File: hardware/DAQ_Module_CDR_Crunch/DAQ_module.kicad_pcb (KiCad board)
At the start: 4 copper layers, 38 x 58.5 mm, 56 parts, among them J1 Conn_01x10_Pin, J3 Conn_01x20_Pin, U1 MCP3564RT-E/ST, U2 MAX31855KASA, U3 MAX31855KASA, U5 TPS70933DBVR, U6 TPS70933DBVR, U7 TPS70933DBVR, U8 MAX31855KASA

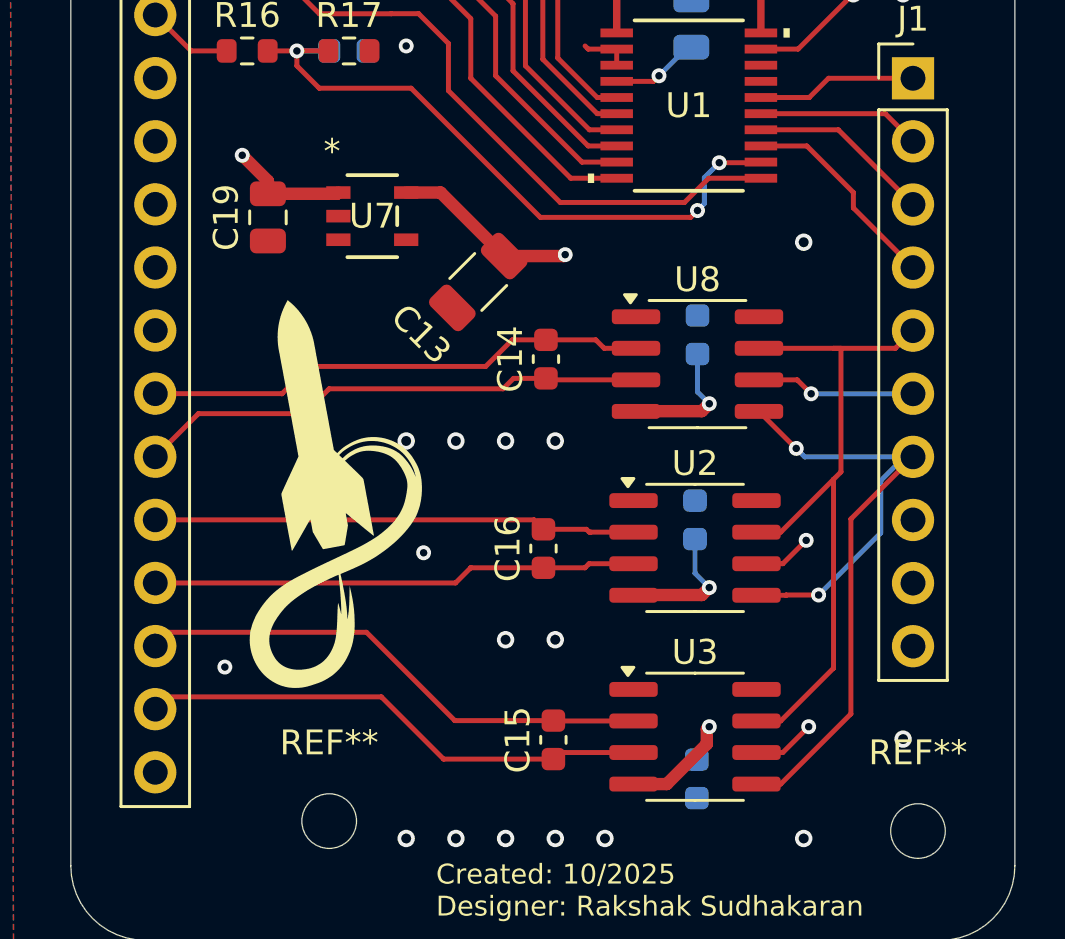
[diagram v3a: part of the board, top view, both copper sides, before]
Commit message: Fixed some traces' layer selection
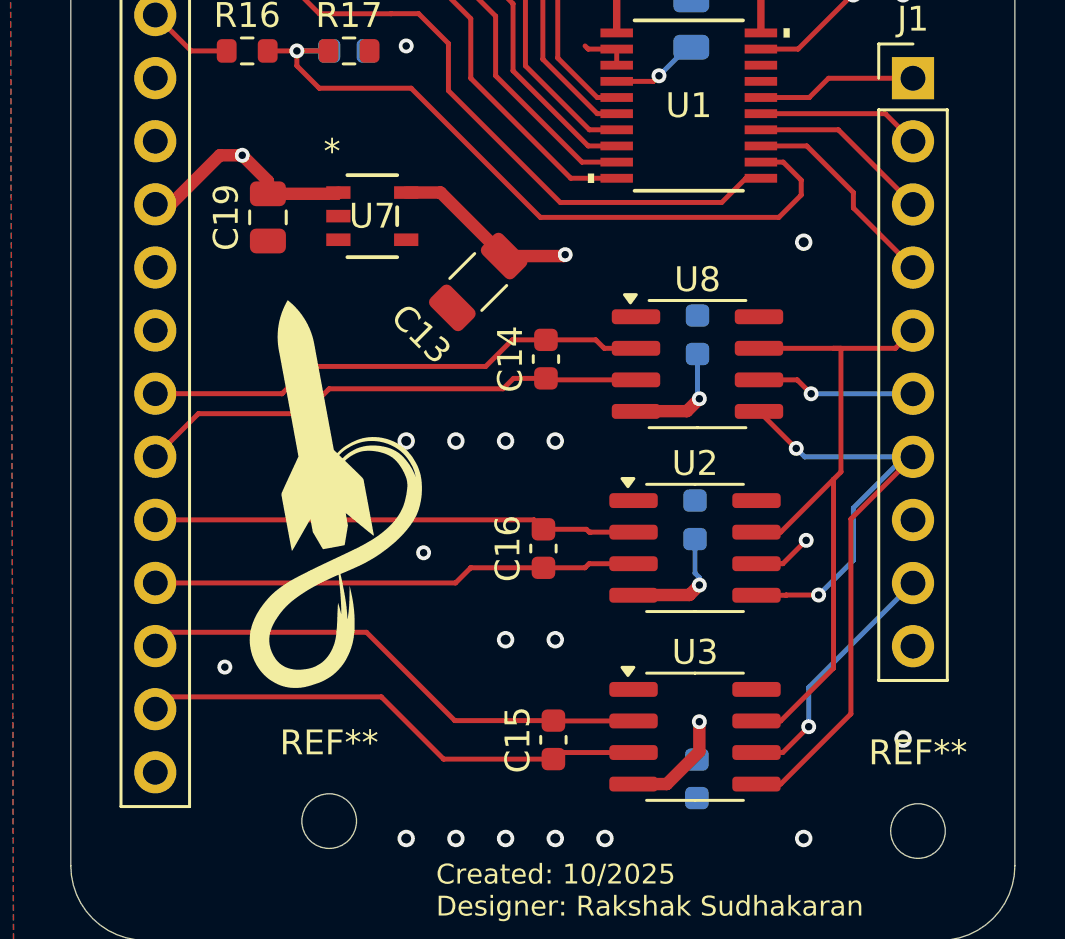
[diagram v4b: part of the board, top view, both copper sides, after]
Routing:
- net /ADC_AI_Filt_7: track 27.1 -> 30.1 mm, vias 3 -> 1
- net Net-(U2-V_{CC}): track 47.9 -> 46.3 mm

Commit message: Updated silkscreen text
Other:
- board text added: "Created: 10/2025 Designer: Rakshak Sudhakaran Board: DAQ Module"
- board text removed: "Created: 10/2025 Designer: Rakshak Sudhakaran"
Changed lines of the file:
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@@
 		(tags "resistor")
 		(property "Reference" "R7"
-			(at 0 -1.43 0)
+			(at 0 1.5 0)
 			(layer "F.SilkS")
 			(effects
@@
 		(tags "resistor")
 		(property "Reference" "R4"
-			(at 0 -1.43 0)
+			(at 0 1.5 0)
 			(layer "F.SilkS")
 			(effects
@@
 		(tags "resistor")
 		(property "Reference" "R2"
-			(at 0 -1.43 0)
+			(at 0 1.5 0)
 			(layer "F.SilkS")
 			(effects
@@
 		(tags "capacitor")
 		(property "Reference" "C2"
-			(at 0 -1.68 0)
+			(at 2.55 1.8 0)
 			(layer "F.SilkS")
 			(effects
@@
 		(tags "resistor")
 		(property "Reference" "R3"
-			(at 0 -1.43 0)
+			(at 0 1.5 0)
 			(layer "F.SilkS")
 			(effects
@@
 		(tags "resistor")
 		(property "Reference" "R9"
-			(at 0 -1.43 0)
+			(at 0 1.5 0)
 			(layer "F.SilkS")
 			(effects
@@
 		(tags "resistor")
 		(property "Reference" "R11"
-			(at 0 -1.43 0)
+			(at 0 1.5 0)
 			(layer "F.SilkS")
 			(effects
@@
 			(at 0 -3.15 0)
 			(layer "F.SilkS")
+			(hide yes)
 			(effects
 				(font
@@
 			(at 0 -3.15 0)
 			(layer "F.SilkS")
+			(hide yes)
 			(effects
 				(font
@@
 			(at 0 -3.15 0)
 			(layer "F.SilkS")
+			(hide yes)
 			(effects
 				(font
@@
 		(tags "resistor")
 		(property "Reference" "R8"
-			(at 0 -1.43 0)
+			(at 0 1.5 0)
 			(layer "F.SilkS")
 			(effects
@@
 		(tags "resistor")
 		(property "Reference" "R12"
-			(at 0 -1.43 0)
+			(at 0 1.5 0)
 			(layer "F.SilkS")
 			(effects
@@
 		(tags "resistor")
 		(property "Reference" "R14"
-			(at 0 -1.43 0)
+			(at 0 1.5 0)
 			(layer "F.SilkS")
 			(effects
@@
 		(tags "resistor")
 		(property "Reference" "R6"
-			(at 0 -1.43 0)
+			(at 0 1.5 0)
 			(layer "F.SilkS")
 			(effects
@@
 		(tags "resistor")
 		(property "Reference" "R15"
-			(at 0 -1.43 0)
+			(at 0 1.5 0)
 			(layer "F.SilkS")
 			(effects
@@
 		(tags "resistor")
 		(property "Reference" "R10"
-			(at 0 -1.43 0)
+			(at 0 1.5 0)
 			(layer "F.SilkS")
 			(effects
@@
 		(tags "resistor")
 		(property "Reference" "R17"
-			(at 0 -1.43 0)
+			(at 0 1.5 0)
 			(layer "F.SilkS")
 			(effects
@@
 		(tags "Through hole pin header THT 1x20 2.54mm single row")
 		(property "Reference" "J3"
-			(at 0 -2.38 0)
+			(at -0.15 51.025 0)
 			(layer "F.SilkS")
 			(effects
@@
 		(tags "resistor")
 		(property "Reference" "R13"
-			(at 0 -1.43 0)
+			(at 0 1.5 0)
 			(layer "F.SilkS")
 			(effects
@@
 		(tags "resistor")
 		(property "Reference" "R5"
-			(at 0 -1.43 0)
+			(at 0 1.5 0)
 			(layer "F.SilkS")
 			(effects
@@
 		(tags "resistor")
 		(property "Reference" "R16"
-			(at 0 -1.43 0)
+			(at 0 1.5 0)
 			(layer "F.SilkS")
 			(effects
@@
 		(tags "capacitor")
 		(property "Reference" "C11"
-			(at 0 1.6 0)
+			(at -2.9 0.525 0)
 			(layer "B.SilkS")
 			(effects
@@
 		(layer "Edge.Cuts")
 	)
-	(gr_text "Created: 10/2025\nDesigner: Rakshak Sudhakaran"
-		(at 174.7 122.3 0)
+	(gr_text "Created: 10/2025\nDesigner: Rakshak Sudhakaran\nBoard: DAQ Module"
+		(at 173.8 121.8 0)
 		(layer "F.SilkS")
 		(effects

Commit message: Finished PCBs
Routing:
- net /ADC_AI_Filt_0: track 33.5 -> 34.2 mm
